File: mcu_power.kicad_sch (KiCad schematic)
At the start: 41 parts, among them U1 MIMXRT1052CVJ5B, U13 TPS62162DSG, Y1 DSC1001BI5-024.0000, Y2 830107834801

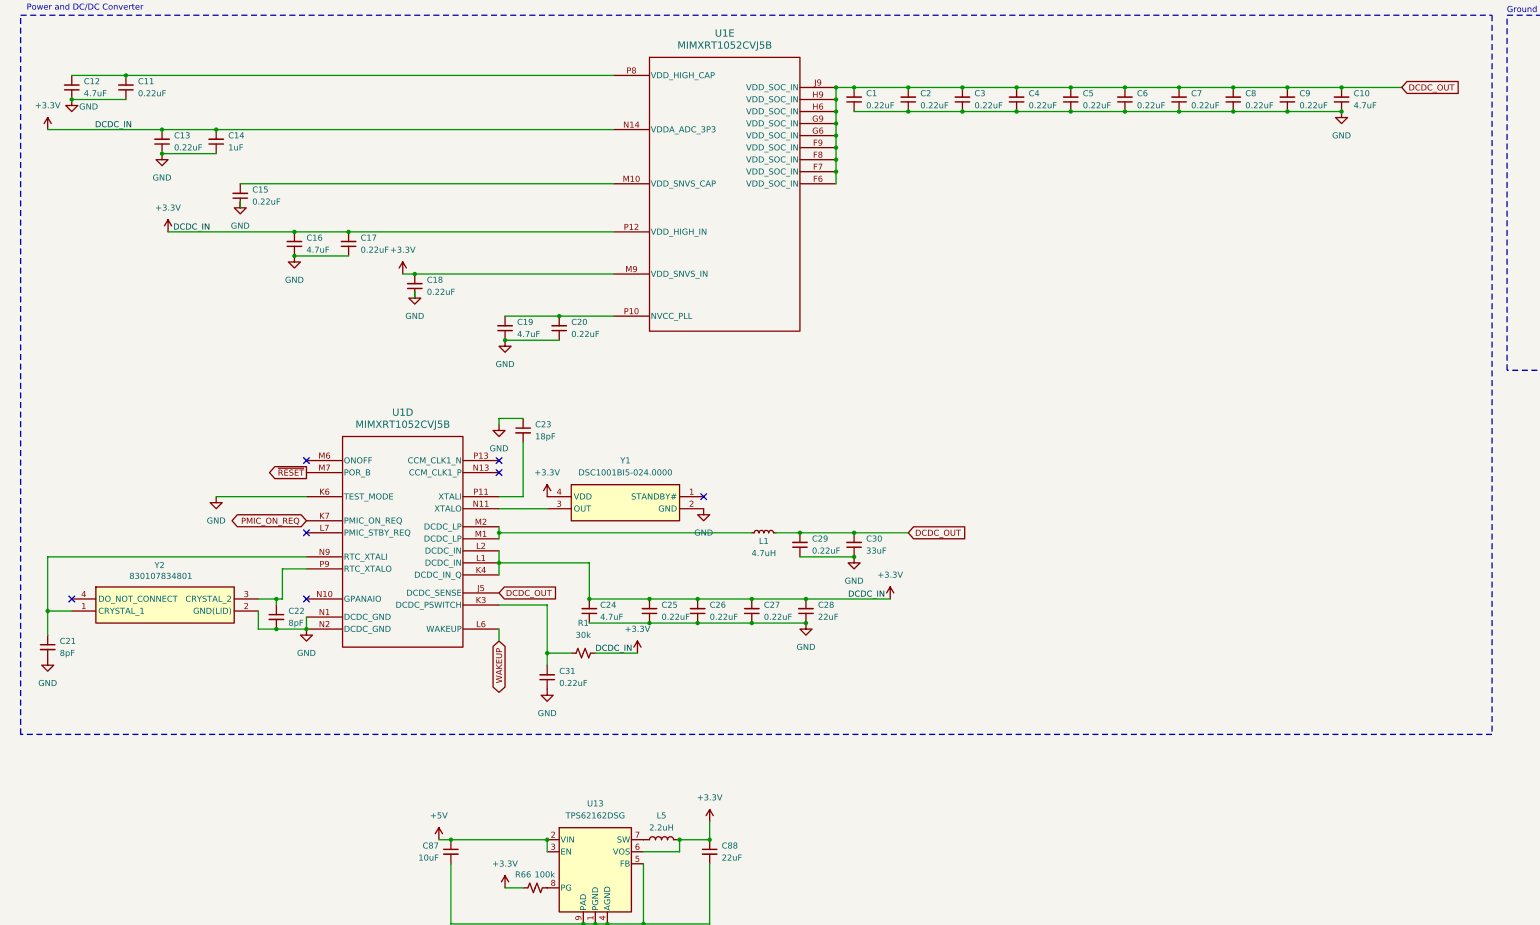
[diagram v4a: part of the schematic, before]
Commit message: added testpoints
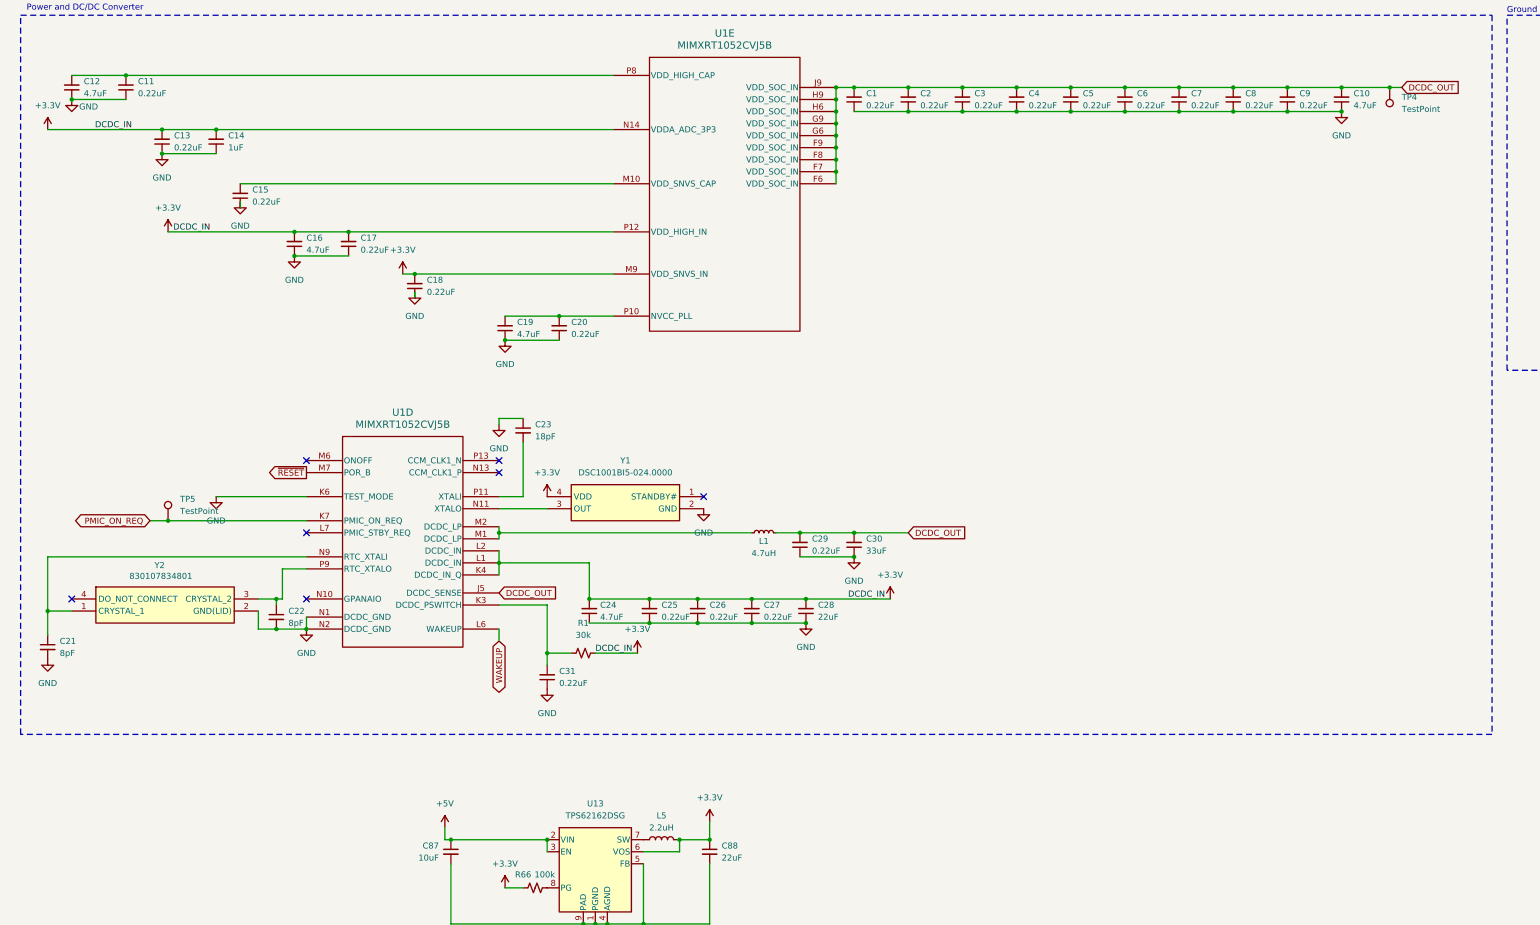
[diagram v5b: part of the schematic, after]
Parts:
- added TP4, TP5: TestPoint, TestPoint:TestPoint_Pad_D1.5mm, symbol Connector:TestPoint
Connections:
- net DCDC_OUT: now also TP4.1
- net PMIC_ON_REQ: now also TP5.1
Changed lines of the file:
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@@
 	)
 	(junction
+		(at 48.26 127)
+		(diameter 0)
+		(color 0 0 0 0)
+	)
+	(junction
 		(at 204.47 35.56)
 		(diameter 0)
@@
 	)
 	(junction
+		(at 306.07 35.56)
+		(diameter 0)
+		(color 0 0 0 0)
+	)
+	(junction
 		(at 149.86 148.59)
 		(diameter 0)
@@
 	(wire
 		(pts
+			(xy 48.26 127) (xy 77.47 127)
+		)
+		(stroke
+			(width 0)
+			(type default)
+		)
+	)
+	(wire
+		(pts
 			(xy 27.94 33.02) (xy 39.37 33.02)
 		)
@@
 	(wire
 		(pts
-			(xy 308.61 35.56) (xy 295.91 35.56)
+			(xy 308.61 35.56) (xy 306.07 35.56)
 		)
 		(stroke
@@
 	(wire
 		(pts
+			(xy 106.68 191.77) (xy 106.68 194.31)
+		)
+		(stroke
+			(width 0)
+			(type default)
+		)
+	)
+	(wire
+		(pts
 			(xy 118.11 105.41) (xy 118.11 106.68)
 		)
@@
 	(wire
 		(pts
-			(xy 189.23 53.34) (xy 189.23 55.88)
+			(xy 106.68 194.31) (xy 107.95 194.31)
 		)
 		(stroke
@@
 	(wire
 		(pts
-			(xy 238.76 40.64) (xy 250.19 40.64)
+			(xy 189.23 53.34) (xy 189.23 55.88)
 		)
 		(stroke
@@
 	(wire
 		(pts
-			(xy 148.59 212.09) (xy 140.97 212.09)
+			(xy 238.76 40.64) (xy 250.19 40.64)
 		)
 		(stroke
@@
 	(wire
 		(pts
-			(xy 162.56 190.5) (xy 162.56 194.31)
+			(xy 148.59 212.09) (xy 140.97 212.09)
 		)
 		(stroke
@@
 	(wire
 		(pts
+			(xy 162.56 190.5) (xy 162.56 194.31)
+		)
+		(stroke
+			(width 0)
+			(type default)
+		)
+	)
+	(wire
+		(pts
 			(xy 138.43 212.09) (xy 140.97 212.09)
 		)
@@
 	(wire
 		(pts
+			(xy 44.45 127) (xy 48.26 127)
+		)
+		(stroke
+			(width 0)
+			(type default)
+		)
+	)
+	(wire
+		(pts
 			(xy 58.42 44.45) (xy 142.24 44.45)
 		)
@@
 	(wire
 		(pts
-			(xy 105.41 194.31) (xy 107.95 194.31)
+			(xy 306.07 35.56) (xy 295.91 35.56)
 		)
 		(stroke
@@
 	(global_label "PMIC_ON_REQ"
 		(shape bidirectional)
-		(at 77.47 127 180)
+		(at 44.45 127 180)
 		(effects
 			(font
@@
 		)
 		(property "Intersheetrefs" "${INTERSHEET_REFS}"
-			(at 77.47 127 0)
+			(at 44.45 127 0)
 			(effects
 				(font
@@
 	)
 	(symbol
+		(lib_id "Connector:TestPoint")
+		(at 306.07 35.56 180)
+		(unit 1)
+		(exclude_from_sim no)
+		(in_bom yes)
+		(on_board yes)
+		(dnp no)
+		(fields_autoplaced yes)
+		(property "Reference" "TP4"
+			(at 308.61 37.5919 0)
+			(effects
+				(font
+					(size 1.27 1.27)
+				)
+				(justify right)
+			)
+		)
+		(property "Value" "TestPoint"
+			(at 308.61 40.1319 0)
+			(effects
+				(font
+					(size 1.27 1.27)
+				)
+				(justify right)
+			)
+		)
+		(property "Footprint" "TestPoint:TestPoint_Pad_D1.5mm"
+			(at 300.99 35.56 0)
+			(effects
+				(font
+					(size 1.27 1.27)
+				)
+				(hide yes)
+			)
+		)
+		(property "Datasheet" "~"
+			(at 300.99 35.56 0)
+			(effects
+				(font
+					(size 1.27 1.27)
+				)
+				(hide yes)
+			)
+		)
+		(property "Description" "test point"
+			(at 306.07 35.56 0)
+			(effects
+				(font
+					(size 1.27 1.27)
+				)
+				(hide yes)
+			)
+		)
+		(pin "1"
+		)
+		(instances
+			(project "RT1050"
+				(path "/dd9d031d-43a1-4442-b493-27451a14e0d9/ef9a9590-bc2d-4a19-b722-cc119a748157"
+					(reference "TP4")
+					(unit 1)
+				)
+			)
+		)
+	)
+	(symbol
 		(lib_id "Device:C_Small")
 		(at 193.04 132.08 180)
@@
 	(symbol
 		(lib_id "power:+5V")
-		(at 105.41 194.31 0)
+		(at 106.68 191.77 0)
 		(unit 1)
 		(exclude_from_sim no)
@@
 		(fields_autoplaced yes)
 		(property "Reference" "#PWR065"
-			(at 105.41 198.12 0)
+			(at 106.68 195.58 0)
 			(effects
 				(font
@@
 		)
 		(property "Value" "+5V"
-			(at 105.41 189.23 0)
+			(at 106.68 186.69 0)
 			(effects
 				(font
@@
 		)
 		(property "Footprint" ""
-			(at 105.41 194.31 0)
+			(at 106.68 191.77 0)
 			(effects
 				(font
@@
 		)
 		(property "Datasheet" ""
-			(at 105.41 194.31 0)
+			(at 106.68 191.77 0)
 			(effects
 				(font
@@
 		)
 		(property "Description" "Power symbol creates a global label with name \"+5V\""
-			(at 105.41 194.31 0)
+			(at 106.68 191.77 0)
 			(effects
 				(font
@@
 				)
 			)
+		)
+	)
+	(symbol
+		(lib_id "Connector:TestPoint")
+		(at 48.26 127 0)
+		(unit 1)
+		(exclude_from_sim no)
+		(in_bom yes)
+		(on_board yes)
+		(dnp no)
+		(fields_autoplaced yes)
+		(property "Reference" "TP5"
+			(at 50.8 122.4279 0)
+			(effects
+				(font
+					(size 1.27 1.27)
+				)
+				(justify left)
+			)
+		)
+		(property "Value" "TestPoint"
+			(at 50.8 124.9679 0)
+			(effects
+				(font
+					(size 1.27 1.27)
+				)
+				(justify left)
+			)
+		)
+		(property "Footprint" "TestPoint:TestPoint_Pad_D1.5mm"
+			(at 53.34 127 0)
+			(effects
+				(font
+					(size 1.27 1.27)
+				)
+				(hide yes)
+			)
+		)
+		(property "Datasheet" "~"
+			(at 53.34 127 0)
+			(effects
+				(font
+					(size 1.27 1.27)
+				)
+				(hide yes)
+			)
+		)
+		(property "Description" "test point"
+			(at 48.26 127 0)
+			(effects
+				(font
+					(size 1.27 1.27)
+				)
+				(hide yes)
+			)
+		)
+		(pin "1"
+		)
+		(instances
+			(project "RT1050"
+				(path "/dd9d031d-43a1-4442-b493-27451a14e0d9/ef9a9590-bc2d-4a19-b722-cc119a748157"
+					(reference "TP5")
+					(unit 1)
+				)
+			)
